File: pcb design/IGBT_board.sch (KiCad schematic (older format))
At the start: 74 parts, among them J1 4-794627-0, Q1 IGBT, Q10 IGBT, Q11 IGBT, Q12 IGBT, Q2 IGBT, Q3 IGBT, Q4 IGBT, Q5 IGBT, Q6 IGBT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

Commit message: Added comments before I forget things, changed X5R to X7R. Updated PCB
Signed-off-by: Marcos Chaparro <mchaparro@paltatech.com>
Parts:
- gave numbers to parts that had none: 6
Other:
- note added: "Sil-pad thermal: SPK4-0.006-00-11.512\nkapton?\nhard anodized aluminum?\ngel immersion? (could help with igbt-heatsink cleareances)"
- note added: "The plan is to design it for 70kw continuous, 200kw peak\n\nSo, at 400v you need 175 Amp per phase (70kw current x 2.5).\nThat is 30A per IGBT\n\nAt 30A, 0.9v Vce = 27W per transistor\naim to 50-50 power losses (switching and sat)\n\nAt 45°C ambient temperature, if we want 75°C\nJunction temp, its a 30°C dT, and we need a\ntotal Rthja < 1.1°C/W\n\n0.15°C/W RthCS = thermal resistance,\ncase to hea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"
- note removed: "Sil-pad thermal: SPK4-0.006-00-11.512"
- note removed: "The plan is to design it for 70kw continuous, 200kw peak\n\nSo, at 400v you need 175 Amp per phase (70kw x 2.5).\nThat is 30A per IGBT\n\nAt 30A, 0.9v Vce = 27W per transistor\n\nAt 45°C ambient temperature, if we want 75°C\nJunction temp, its a 30°C dT, and we need a\ntotal Rthja < 1.1°C/W\n\n0.15°C/W RthCS = thermal resistance,\ncase to heat sink (from the device data sheet). \n\n\n\n\n\n\n"
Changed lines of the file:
@@
 	1    0    0    -1
 $EndComp
-Text Notes 4800 8200 0    50   ~ 0
-The plan is to design it for 70kw continuous, 200kw peak\n\nSo, at 400v you need 175 Amp per phase (70kw x 2.5).\nThat is 30A per IGBT\n\nAt 30A, 0.9v Vce = 27W per transistor\n\nAt 45°C ambient temperature, if we want 75°C\nJunction temp, its a 30°C dT, and we need a\ntotal Rthja < 1.1°C/W\n\n0.15°C/W RthCS = thermal resistance,\ncase to heat sink (from the device data sheet). \n\n\n\n\n\n\n
-Text Notes 7000 6950 0    60   ~ 0
-Sil-pad thermal: SPK4-0.006-00-11.512
+Text Notes 4800 8250 0    50   ~ 0
+The plan is to design it for 70kw continuous, 200kw peak\n\nSo, at 400v you need 175 Amp per phase (70kw current  x 2.5).\nThat is 30A per IGBT\n\nAt 30A, 0.9v Vce = 27W per transistor\naim to 50-50 power losses (switching and sat)\n\nAt 45°C ambient temperature, if we want 75°C\nJunction temp, its a 30°C dT, and we need a\ntotal Rthja < 1.1°C/W\n\n0.15°C/W RthCS = thermal resistance,\ncase to heat sink (from the device data sheet). \n\n\n\n\n\n\n
+Text Notes 7400 7000 0    60   ~ 0
+Sil-pad thermal: SPK4-0.006-00-11.512\nkapton?\nhard anodized aluminum?\ngel immersion? (could help with igbt-heatsink cleareances)
 Text Notes 9200 1450 0    40   ~ 0
 Capacitors must be ably tu supply roughly 65% of battery\nsupplied current, so its important to have enough rms\ncurrent in the cap bank.\nIn this case, if we plan for 200kW at 500A, we should expect\na total RMS current of 325A in the capacitors.\nWe have 16uF*7*3 = 336uF\n14Arms per cap -> 98Arms per module, 296Arms per inverter
@@
 RESET
 $Comp
-L GND #PWR4
+L GND #PWR01
 U 1 1 5831A3A1
 P 2150 1800
-F 0 "#PWR4" H 2150 1800 30  0001 C CNN
+F 0 "#PWR01" H 2150 1800 30  0001 C CNN
 F 1 "GND" H 2150 1730 30  0001 C CNN
 F 2 "" H 2150 1800 60  0000 C CNN
@@
 $EndComp
 $Comp
-L GND #PWR5
+L GND #PWR02
 U 1 1 58386BF0
 P 2800 4550
-F 0 "#PWR5" H 2800 4550 30  0001 C CNN
+F 0 "#PWR02" H 2800 4550 30  0001 C CNN
 F 1 "GND" H 2800 4480 30  0001 C CNN
 F 2 "" H 2800 4550 60  0000 C CNN
@@
 $EndComp
 $Comp
-L GND #PWR2
+L GND #PWR03
 U 1 1 58387D39
 P 1850 6600
-F 0 "#PWR2" H 1850 6600 30  0001 C CNN
+F 0 "#PWR03" H 1850 6600 30  0001 C CNN
 F 1 "GND" H 1850 6530 30  0001 C CNN
 F 2 "" H 1850 6600 60  0000 C CNN
@@
 24v
 $Comp
-L GND #PWR1
+L GND #PWR04
 U 1 1 583AB791
 P 1750 3150
-F 0 "#PWR1" H 1750 3150 30  0001 C CNN
+F 0 "#PWR04" H 1750 3150 30  0001 C CNN
 F 1 "GND" H 1750 3080 30  0001 C CNN
 F 2 "" H 1750 3150 60  0000 C CNN
@@
 $EndComp
 $Comp
-L GND #PWR3
+L GND #PWR05
 U 1 1 583AF86E
 P 2050 2050
-F 0 "#PWR3" H 2050 2050 30  0001 C CNN
+F 0 "#PWR05" H 2050 2050 30  0001 C CNN
 F 1 "GND" H 2050 1980 30  0001 C CNN
 F 2 "" H 2050 2050 60  0000 C CNN
@@
 Connection ~ 4400 6650
 $Comp
-L GND #PWR6
+L GND #PWR06
 U 1 1 585B4E01
 P 2850 6750
-F 0 "#PWR6" H 2850 6750 30  0001 C CNN
+F 0 "#PWR06" H 2850 6750 30  0001 C CNN
 F 1 "GND" H 2850 6680 30  0001 C CNN
 F 2 "" H 2850 6750 60  0000 C CNN
@@
 	2850 6350 2950 6350
 $Comp
-L MOUNTING_HOLE HOLE?
+L MOUNTING_HOLE HOLE1
 U 1 1 585C45CA
 P 10150 6500
-F 0 "HOLE?" H 10277 6553 60  0000 L CNN
+F 0 "HOLE1" H 10277 6553 60  0000 L CNN
 F 1 "MH" H 10277 6447 60  0000 L CNN
 F 2 "" H 10150 6500 60  0000 C CNN
@@
 NoConn ~ 9950 6500
 $Comp
-L MOUNTING_HOLE HOLE?
+L MOUNTING_HOLE HOLE2
 U 1 1 585C56CA
 P 10150 6750
-F 0 "HOLE?" H 10277 6803 60  0000 L CNN
+F 0 "HOLE2" H 10277 6803 60  0000 L CNN
 F 1 "MH" H 10277 6697 60  0000 L CNN
 F 2 "" H 10150 6750 60  0000 C CNN
@@
 $EndComp
 $Comp
-L MOUNTING_HOLE HOLE?
+L MOUNTING_HOLE HOLE4
 U 1 1 585C5DBC
 P 10700 6750
-F 0 "HOLE?" H 10827 6803 60  0000 L CNN
+F 0 "HOLE4" H 10827 6803 60  0000 L CNN
 F 1 "MH" H 10827 6697 60  0000 L CNN
 F 2 "" H 10700 6750 60  0000 C CNN
@@
 $EndComp
 $Comp
-L HV #SYM?
+L HV #SYM1
 U 1 1 585C631E
 P 4000 2300
-F 0 "#SYM?" H 4000 2300 60  0001 C CNN
+F 0 "#SYM1" H 4000 2300 60  0001 C CNN
 F 1 "HV" H 4000 2300 60  0001 C CNN
 F 2 "" H 3900 2200 60  0000 C CNN
@@
 $EndComp
 $Comp
-L MOUNTING_HOLE HOLE?
+L MOUNTING_HOLE HOLE3
 U 1 1 585C7B75
 P 10700 6500
-F 0 "HOLE?" H 10827 6553 60  0000 L CNN
+F 0 "HOLE3" H 10827 6553 60  0000 L CNN
 F 1 "MH" H 10827 6447 60  0000 L CNN
 F 2 "" H 10700 6500 60  0000 C CNN
@@
 NoConn ~ 10500 6500
 $Comp
-L C-0603 C?
+L C-0603 C77
 U 1 1 585F404D
 P 1150 2300
-F 0 "C?" H 1262 2346 50  0000 L CNN
+F 0 "C77" H 1262 2346 50  0000 L CNN
 F 1 "100pF" H 1262 2255 50  0000 L CNN
 F 2 "IPC7351-Nominal:CAPC1608X55" H 1150 2300 50  0001 C CNN
@@
 $EndComp
 $Comp
-L C-0603 C?
+L C-0603 C82
 U 1 1 585F49C0
 P 2300 2300
-F 0 "C?" H 2412 2346 50  0000 L CNN
+F 0 "C82" H 2412 2346 50  0000 L CNN
 F 1 "100pF" H 2412 2255 50  0000 L CNN
 F 2 "IPC7351-Nominal:CAPC1608X55" H 2300 2300 50  0001 C CNN
@@
 Connection ~ 2300 1950
 $Comp
-L GND #PWR?
+L GND #PWR07
 U 1 1 585F4F4E
 P 2300 2400
-F 0 "#PWR?" H 2300 2400 30  0001 C CNN
+F 0 "#PWR07" H 2300 2400 30  0001 C CNN
 F 1 "GND" H 2300 2330 30  0001 C CNN
 F 2 "" H 2300 2400 60  0000 C CNN
@@
 $EndComp
 $Comp
-L GND #PWR?
+L GND #PWR08
 U 1 1 585F510F
 P 1150 2400
-F 0 "#PWR?" H 1150 2400 30  0001 C CNN
+F 0 "#PWR08" H 1150 2400 30  0001 C CNN
 F 1 "GND" H 1150 2330 30  0001 C CNN
 F 2 "" H 1150 2400 60  0000 C CNN

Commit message: Power supply sync input. And more comments
Signed-off-by: Marcos Chaparro <mchaparro@paltatech.com>
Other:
- note added: "PHASE LEG IGBT MODULE"
- note removed: "HALF BRIDGE IGBT MODULE"
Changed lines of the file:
@@
 Text Label 1700 4850 0    50   ~ 0
 PWR_GOOD
-Text Notes 2050 1300 0    300  ~ 60
-HALF BRIDGE IGBT MODULE
+Text Notes 1000 1250 0    300  ~ 60
+PHASE LEG IGBT MODULE
 Text GLabel 2400 2700 2    50   Input ~ 0
 3.3v

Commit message: Changed power supply from 15/-8V to +15/-15V se we can make better use uf programmable -VEE. Changed connector to 14pos. Connected some missing signals. Updated layout
Signed-off-by: Marcos Chaparro <mchaparro@paltatech.com>
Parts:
- removed C50: 100nF, IPC7351-Nominal:CAPC1608X55, symbol C-0603
- removed J1: 4-794627-0, paltatech:TE-4-794627-0, symbol 4-794627-0
- removed U4: NAND, smd-semi:SOT-23-5, symbol 741G00-SOT23
- added J1: 61001421121, paltatech:conn-2x7-2.54mm_SMD, symbol CONN-100MIL-M-2x7
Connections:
- net labels added: PWM_N, PWM_P, SYNC, VEE_CTRL, V_phase+, V_phase-
- net labels removed: IN_BOTTOM, IN_TOP
- wire segments 206 -> 213
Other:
- note removed: "If both PWM inputs are high,\nwe trigger the FAULT signal\nwhich turns off the whole\ninverter and will be latched\nuntil a reset is issued"
- moved on the sheet: C51, C52, C77, C82, D19, DS1, DS2, DS3, F1, R51, R52, R53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

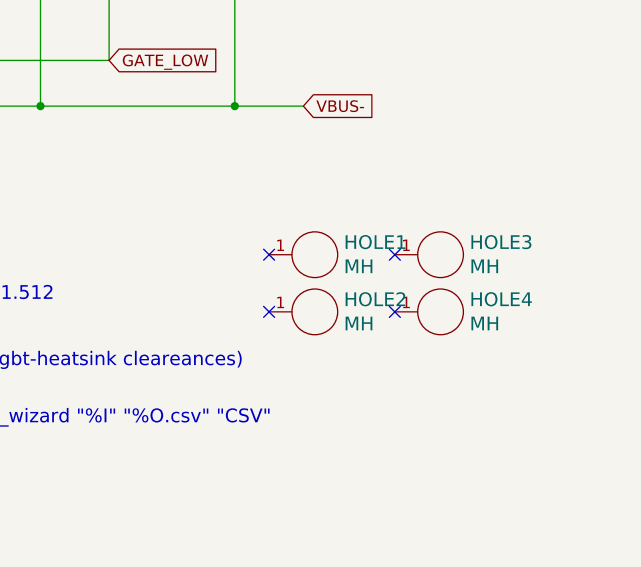
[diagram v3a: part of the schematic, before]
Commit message: For some reasong eyrie needs the schematics and cache file synced
Signed-off-by: Marcos Chaparro <mchaparro@paltatech.com>
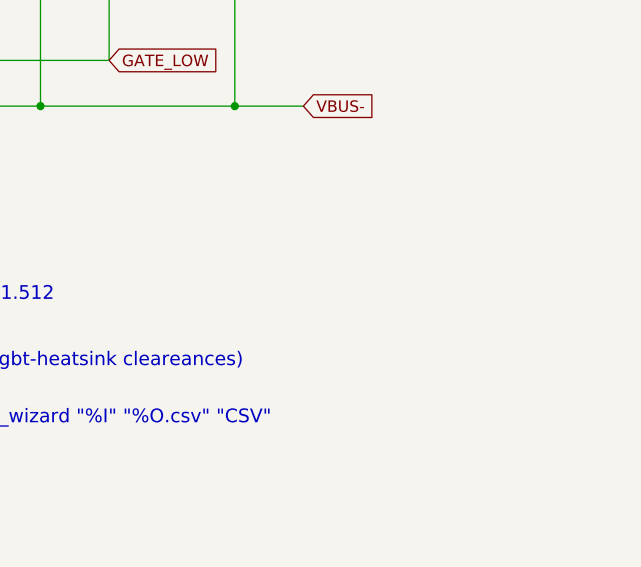
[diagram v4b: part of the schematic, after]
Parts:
- removed HOLE1, HOLE2, HOLE3, HOLE4: MH, symbol MOUNTING_HOLE
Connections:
- no-connect marks 5 -> 1
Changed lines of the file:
@@
 	2850 6350 2950 6350
-$Comp
-L MOUNTING_HOLE HOLE1
-U 1 1 585C45CA
-P 10150 6500
-F 0 "HOLE1" H 10277 6553 60  0000 L CNN
-F 1 "MH" H 10277 6447 60  0000 L CNN
-F 2 "" H 10150 6500 60  0000 C CNN
-F 3 "" H 10150 6500 60  0000 C CNN
-	1    10150 6500
-	1    0    0    -1
-$EndComp
-NoConn ~ 9950 6500
-$Comp
-L MOUNTING_HOLE HOLE2
-U 1 1 585C56CA
-P 10150 6750
-F 0 "HOLE2" H 10277 6803 60  0000 L CNN
-F 1 "MH" H 10277 6697 60  0000 L CNN
-F 2 "" H 10150 6750 60  0000 C CNN
-F 3 "" H 10150 6750 60  0000 C CNN
-	1    10150 6750
-	1    0    0    -1
-$EndComp
-$Comp
-L MOUNTING_HOLE HOLE4
-U 1 1 585C5DBC
-P 10700 6750
-F 0 "HOLE4" H 10827 6803 60  0000 L CNN
-F 1 "MH" H 10827 6697 60  0000 L CNN
-F 2 "" H 10700 6750 60  0000 C CNN
-F 3 "" H 10700 6750 60  0000 C CNN
-	1    10700 6750
-	1    0    0    -1
-$EndComp
 $Comp
 L HV #SYM1
@@
 $EndComp
 $Comp
-L MOUNTING_HOLE HOLE3
-U 1 1 585C7B75
-P 10700 6500
-F 0 "HOLE3" H 10827 6553 60  0000 L CNN
-F 1 "MH" H 10827 6447 60  0000 L CNN
-F 2 "" H 10700 6500 60  0000 C CNN
-F 3 "" H 10700 6500 60  0000 C CNN
-	1    10700 6500
-	1    0    0    -1
-$EndComp
-NoConn ~ 9950 6750
-NoConn ~ 10500 6750
-NoConn ~ 10500 6500
-$Comp
 L C-0603 C77

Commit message: Added CERN Open Hardware Licence ("CERN OHL") version 1.2 documents
Signed-off-by: Marcos Chaparro <mchaparro@paltatech.com>
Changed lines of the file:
@@
 Sheet 1 7
 Title "IGBT module"
-Date "2016-11-24"
+Date "2017-01-17"
 Rev "A"
-Comp "PALTA TECH S.A."
-Comment1 ""
+Comp "Copyright PALTA TECH S.A."
+Comment1 "This documentation describes Open Hardware and is licensed under the CERN OHL v. 1.2"
 Comment2 ""
 Comment3 ""
@@
 L OSHW-SCHEM-PCB10mm SYM1
 U 1 1 583B5122
-P 7150 7200
-F 0 "SYM1" H 7284 7200 50  0001 L CNN
-F 1 "OSHW-SCHEM-PCB10mm" H 7150 7150 50  0001 C CNN
-F 2 "w_logo:Logo_silk_OSHW_12x13mm" H 7200 7100 50  0001 C CNN
-F 3 "" H 7150 7200 50  0000 C CNN
-	1    7150 7200
-	1    0    0    -1
-$EndComp
+P 7100 7150
+F 0 "SYM1" H 7234 7150 50  0001 L CNN
+F 1 "OSHW-SCHEM-PCB10mm" H 7100 7100 50  0001 C CNN
+F 2 "w_logo:Logo_silk_OSHW_12x13mm" H 7150 7050 50  0001 C CNN
+F 3 "" H 7100 7150 50  0000 C CNN
+	1    7100 7150
+	1    0    0    -1
+$EndComp

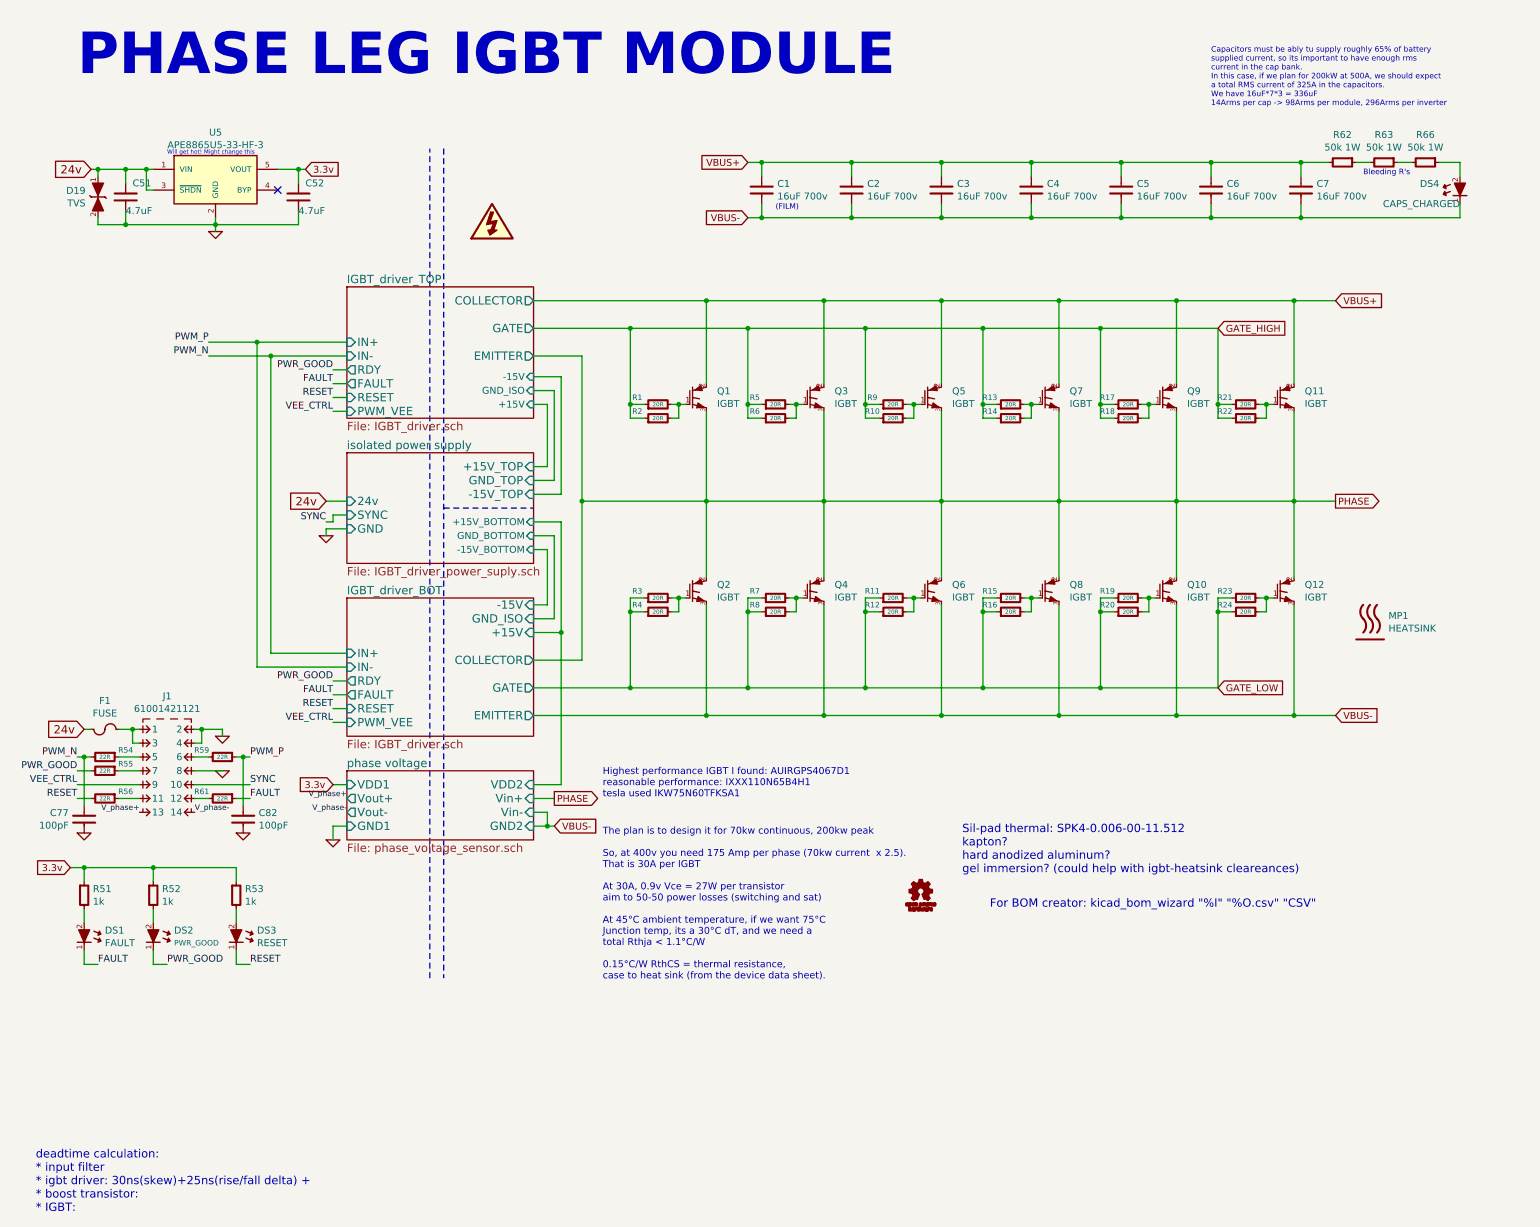
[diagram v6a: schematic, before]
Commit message: Added current sensor connector. Layout is now symmetrical
Signed-off-by: Marcos Chaparro <mchaparro@paltatech.com>
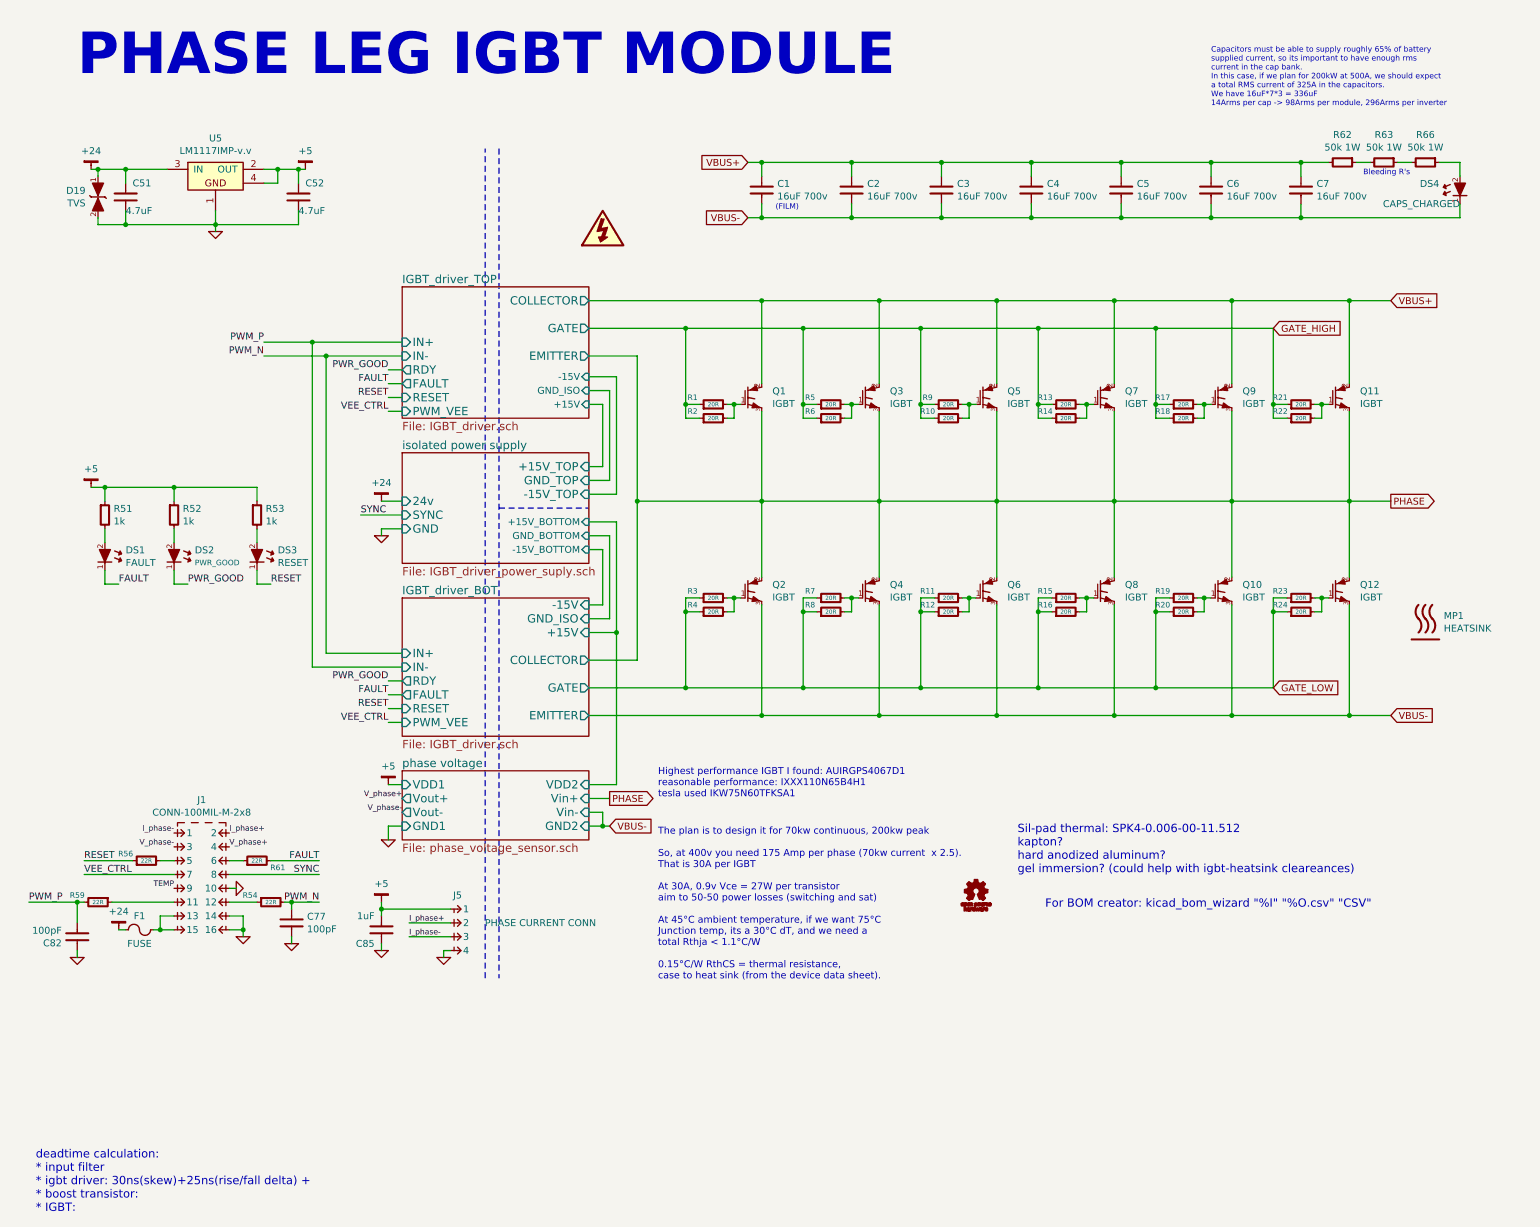
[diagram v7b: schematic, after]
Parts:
- removed J1: 61001421121, paltatech:conn-2x7-2.54mm_SMD, symbol CONN-100MIL-M-2x7
- removed R55: 22R, IPC7351-Nominal:RESC1608X50, symbol R-0603
- removed U5: APE8865U5-33-HF-3, SC-70-5, symbol APE8865U5-33-HF-3
- added C85: 1uF, IPC7351-Nominal:CAPC1608X55, symbol C-0603
- added J1: CONN-100MIL-M-2x8, conn-100mil:CONN-100MIL-M-2x8, symbol CONN-100MIL-M-2x8
- added J5: PHASE CURRENT CONN, paltatech:TE-292227-4, symbol CONN-100MIL-M-1x4
- added U5: LM1117IMP-v.v, smd-semi:SOT-223, symbol LM1117IMP-v.v
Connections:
- net FAULT: now also R61.2; no longer R61.1
- net GND: now also C82.1, C85.1, J1.10, J1.14, J1.16, J5.4, U5.1; no longer C82.2
- net PWM_P: now also C82.2, R59.2; no longer C82.1, R59.1
- net RESET: now also R56.1; no longer R56.2
- net SYNC: now also J1.8
- net VEE_CTRL: now also J1.7
- net V_phase+: now also J1.4
- net V_phase-: now also J1.3
- net +24: now reaches F1.2
- net +24: now also C51.1, D19.1 (A1), U5.3 (IN)
- net at R54.1: now also J1.12
- removed net 24v: C51.1, D19.1 (A1), F1.1
- net 3.3v renamed +5
- net +5: now also C85.2, J5.1, U5.2 (OUT), U5.4
- new net: F1.1, J1.13, J1.15
- new net: J1.5, R56.2
- new net: J1.11, R59.1
- new net: J1.6, R61.1
- new net I_phase+: J1.2, J5.2
- new net I_phase-: J1.1, J5.3
- new net TEMP: J1.9
- no-connect marks 1 -> 0
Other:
- note added: "Capacitors must be able to supply roughly 65% of battery\nsupplied current, so its important to have enough rms\ncurrent in the cap bank.\nIn this case, if we plan for 200kW at 500A, we should expect\na total RMS current of 325A in the capacitors.\nWe have 16uF*7*3 = 336uF\n14Arms per cap -> 98Arms per module, 296Arms per inverter"
- note removed: "Capacitors must be ably tu supply roughly 65% of battery\nsupplied current, so its important to have enough rms\ncurrent in the cap bank.\nIn this case, if we plan for 200kW at 500A, we should expect\na total RMS current of 325A in the capacitors.\nWe have 16uF*7*3 = 336uF\n14Arms per cap -> 98Arms per module, 296Arms per inverter"
- note removed: "Will get hot! Might change this"
- moved on the sheet: C77, C82, DS1, DS2, DS3, F1, MP1, Q1, Q10, Q11, Q12, Q2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
